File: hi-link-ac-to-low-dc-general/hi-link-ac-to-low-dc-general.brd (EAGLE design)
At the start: 50 x 65 mm, 10 parts

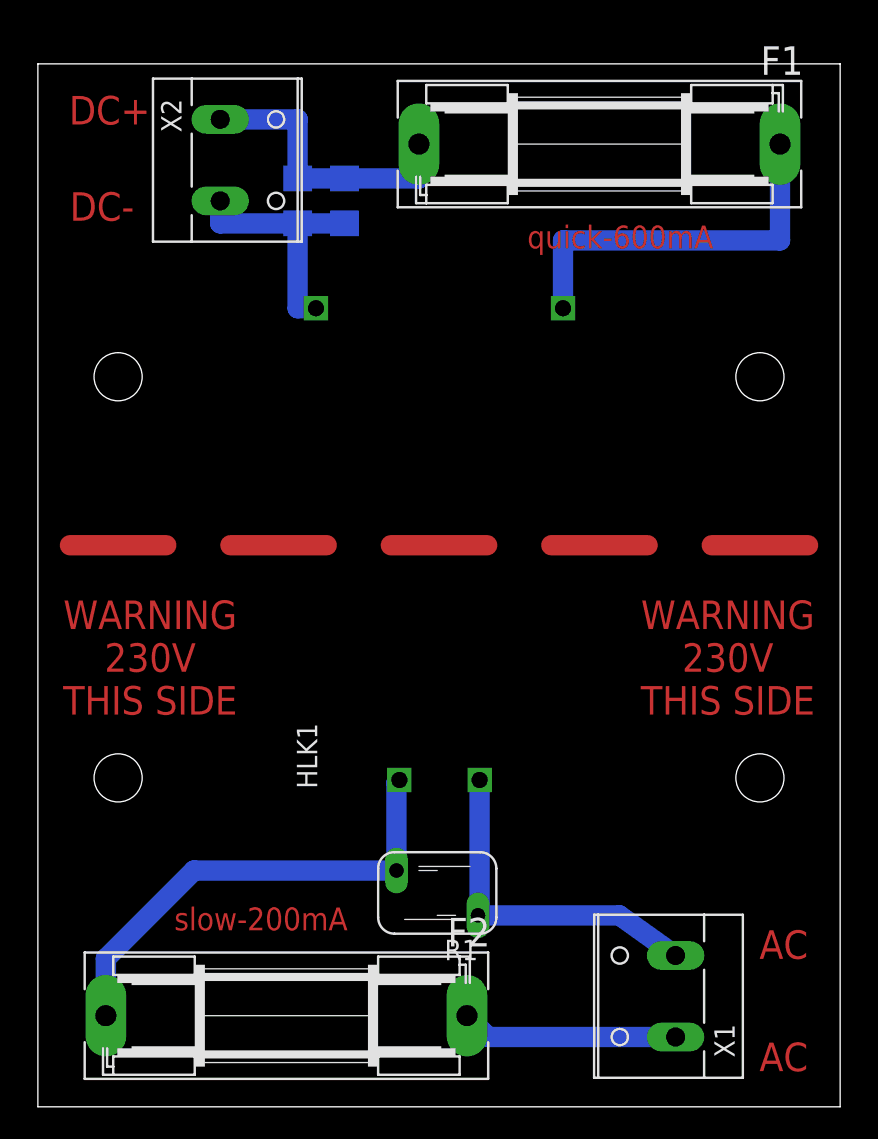
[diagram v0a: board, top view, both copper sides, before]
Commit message: hi-link-ac-to-low-dc-general update text layer to silk
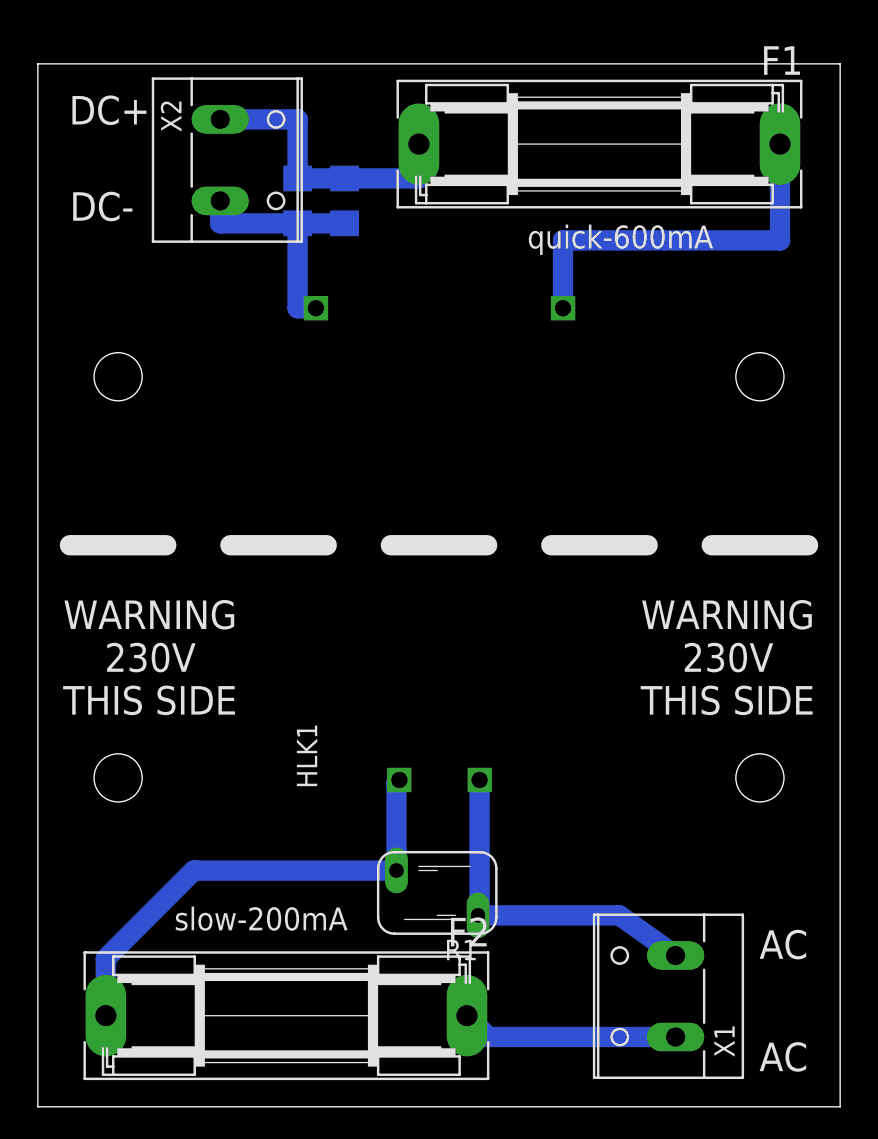
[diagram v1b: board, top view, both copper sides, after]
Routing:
- net N$7: track 30.0 -> 0.00 mm
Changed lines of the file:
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@@
 <layer number="116" name="Patch_BOT" color="7" fill="1" visible="yes" active="yes"/>
 <layer number="118" name="Rect_Pads" color="7" fill="1" visible="yes" active="yes"/>
-<layer number="121" name="_tsilk" color="7" fill="1" visible="no" active="yes"/>
-<layer number="122" name="_bsilk" color="7" fill="1" visible="no" active="yes"/>
+<layer number="121" name="_tsilk" color="7" fill="1" visible="yes" active="yes"/>
+<layer number="122" name="_bsilk" color="7" fill="1" visible="yes" active="yes"/>
 <layer number="123" name="tTestmark" color="7" fill="1" visible="yes" active="yes"/>
 <layer number="124" name="bTestmark" color="7" fill="1" visible="yes" active="yes"/>
@@
 <wire x1="50" y1="65" x2="0" y2="65" width="0" layer="20"/>
 <wire x1="0" y1="65" x2="0" y2="0" width="0" layer="20"/>
-<text x="48" y="11" size="1.778" layer="1" rot="R180">AC</text>
-<text x="48" y="4" size="1.778" layer="1" rot="R180">AC</text>
-<text x="7" y="63" size="1.778" layer="1" rot="R180">DC+</text>
-<text x="6" y="57" size="1.778" layer="1" rot="R180">DC-</text>
-<text x="30.5" y="53.5" size="1.4224" layer="1">quick-600mA</text>
-<text x="8.5" y="11" size="1.4224" layer="1">slow-200mA</text>
-<text x="7" y="28" size="1.778" layer="1" rot="R180" align="center">WARNING
+<text x="48" y="11" size="1.778" layer="121" rot="R180">AC</text>
+<text x="48" y="4" size="1.778" layer="121" rot="R180">AC</text>
+<text x="7" y="63" size="1.778" layer="121" rot="R180">DC+</text>
+<text x="6" y="57" size="1.778" layer="121" rot="R180">DC-</text>
+<text x="30.5" y="53.5" size="1.4224" layer="121">quick-600mA</text>
+<text x="8.5" y="11" size="1.4224" layer="121">slow-200mA</text>
+<text x="7" y="28" size="1.778" layer="121" rot="R180" align="center">WARNING
 230V
 THIS SIDE</text>
-<text x="43" y="28" size="1.778" layer="1" rot="R180" align="center">WARNING
+<text x="43" y="28" size="1.778" layer="121" rot="R180" align="center">WARNING
 230V
 THIS SIDE</text>
+<wire x1="2" y1="35" x2="8" y2="35" width="1.27" layer="121"/>
+<wire x1="12" y1="35" x2="18" y2="35" width="1.27" layer="121"/>
+<wire x1="22" y1="35" x2="28" y2="35" width="1.27" layer="121"/>
+<wire x1="32" y1="35" x2="38" y2="35" width="1.27" layer="121"/>
+<wire x1="42" y1="35" x2="48" y2="35" width="1.27" layer="121"/>
 </plain>
 <attributes>
@@
 <wire x1="27.53" y1="12.033" x2="27.53" y2="20.37" width="1.27" layer="16"/>
 </signal>
-<signal name="N$7">
-<wire x1="12" y1="35" x2="18" y2="35" width="1.27" layer="1"/>
-<wire x1="22" y1="35" x2="28" y2="35" width="1.27" layer="1"/>
-<wire x1="32" y1="35" x2="38" y2="35" width="1.27" layer="1"/>
-<wire x1="42" y1="35" x2="48" y2="35" width="1.27" layer="1"/>
-<wire x1="2" y1="35" x2="8" y2="35" width="1.27" layer="1"/>
-</signal>
 </signals>
